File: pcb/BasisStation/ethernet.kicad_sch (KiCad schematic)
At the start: 35 parts, among them T1 7499011121A, U7 W5500, Y1 25 MHz

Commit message: v0.00.001 feat(SHBS-17): Teilenummern fuer 29 Positionen in den Schaltplan uebernommen
Die vom Bediener freigegebenen Teilevorschlaege (Hausstandard Passivteile, LEDs, Q1-Q4, F1, FB1) stehen jetzt als Felder Manufacturer, Manufacturer_Part_Number und Mouser Part Number an 58 Instanzen. F1-Wert von Fuse auf 1.1A gesetzt. Gegenprobe: keine Felder verloren, Netzliste identisch (102 Netze), ERC 0 Fehler.

Stueckliste gruppiert jetzt nach Herstellerteilenummer (Werte sind uneinheitlich geschrieben): 44 Positionen, alle lieferbar, 47,78 EUR. PROPOSED_PARTS geleert, Hausstandard in hardware.md dokumentiert, Bestellteile in power_supply.md aktualisiert.

Co-Authored-By: Claude Opus 5.5 <noreply@anthropic.com>
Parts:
- C16, C17, C18, C19, C20, C21, C22: Manufacturer (none) -> YAGEO; Manufacturer_Part_Number (none) -> CC0805KRX7R9BB104; Mouser Part Number (none) -> 603-CC805KRX7R9BB104
- C23: Manufacturer (none) -> Samsung; Manufacturer_Part_Number (none) -> CL21A475KAQNNNE; Mouser Part Number (none) -> 187-CL21A475KAQNNNE
- C24, C31: Manufacturer (none) -> YAGEO; Manufacturer_Part_Number (none) -> CC0805KRX7R9BB103; Mouser Part Number (none) -> 603-CC805KRX7R9BB103
- C25, C26: Manufacturer (none) -> YAGEO; Manufacturer_Part_Number (none) -> CC0805JRNPO9BN270; Mouser Part Number (none) -> 603-CC805JRNPO9BN270
- C27: Manufacturer (none) -> Samsung; Manufacturer_Part_Number (none) -> CL21B106KOQNNNE; Mouser Part Number (none) -> 187-CL21B106KOQNNNE
- C28: Manufacturer (none) -> KEMET; Manufacturer_Part_Number (none) -> C1206C102KGRACTU; Mouser Part Number (none) -> 80-C1206C102KGR
- C29, C30: Manufacturer (none) -> YAGEO; Manufacturer_Part_Number (none) -> CC0805KRX7R9BB682; Mouser Part Number (none) -> 603-CC805KRX7R9BB682
- C32: Manufacturer (none) -> Samsung; Manufacturer_Part_Number (none) -> CL21B223KBANNNC; Mouser Part Number (none) -> 187-CL21B223KBANNNC
- FB1: Manufacturer (none) -> Murata; Manufacturer_Part_Number (none) -> BLM21PG601SN1D; Mouser Part Number (none) -> 81-BLM21PG601SN1D
- R27: Manufacturer (none) -> YAGEO; Manufacturer_Part_Number (none) -> RC0805FR-0712K4L; Mouser Part Number (none) -> 603-RC0805FR-0712K4L
- R28, R29, R30, R31, R32: Manufacturer (none) -> YAGEO; Manufacturer_Part_Number (none) -> RC0805FR-0710KL; Mouser Part Number (none) -> 603-RC0805FR-0710KL
- R33, R34: Manufacturer (none) -> YAGEO; Manufacturer_Part_Number (none) -> RC0805FR-07220RL; Mouser Part Number (none) -> 603-RC0805FR-07220RL
- R35: Manufacturer (none) -> YAGEO; Manufacturer_Part_Number (none) -> RC0805JR-070RL; Mouser Part Number (none) -> 603-RC0805JR-070RL
- R36, R37, R39, R40: Manufacturer (none) -> YAGEO; Manufacturer_Part_Number (none) -> RC0805FR-0749R9L; Mouser Part Number (none) -> 603-RC0805FR-0749R9L
- R38: Manufacturer (none) -> YAGEO; Manufacturer_Part_Number (none) -> RC0805FR-0710RL; Mouser Part Number (none) -> 603-RC0805FR-0710RL

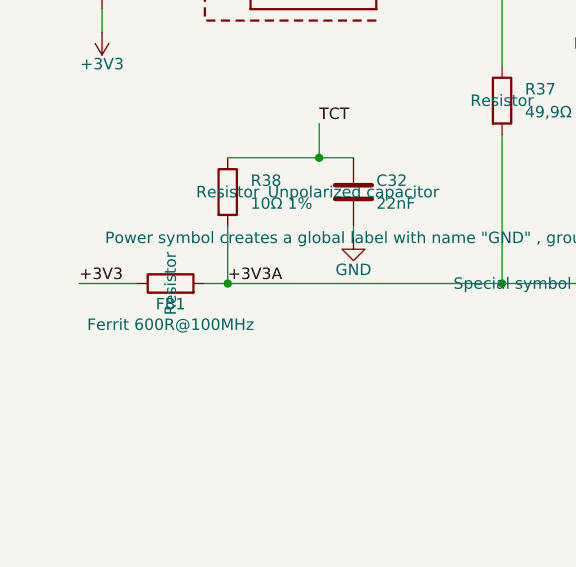
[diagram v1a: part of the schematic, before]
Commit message: v0.00.001 fix(SHBS-16): D10-Verpolung behoben, LED-Symbole vereinheitlicht, FB1 und J6 bereinigt
Footprint WL-TMRC_3MM hatte Pad 1 = Anode, Device:LED hat Pin 1 = Kathode: D10 lag mit der Kathode an +3V3 und haette nie geleuchtet. Footprint auf Pad 1 = K / Pad 2 = A umnummeriert (wie WL-TMRW_3MM), Wuerth-Symbol mitgezogen. D7 von WL-TMRC_3MM auf Device:LED, so platziert, dass K/A auf den bisherigen Drahtenden liegen. FB1 auf Device:FerriteBead, J6-Wert auf 61200621621.

Gegenprobe: ERC 0 Fehler; Netzliste mit gleichen Bauteilen je Netz, nur D7-Pinnummern getauscht; Polaritaet aller vier LEDs auf Pad-Ebene geprueft. Beim naechsten PCB-Abgleich Footprint von D7/D10 aus der Bibliothek aktualisieren. Task 0042 abgeschlossen.

Co-Authored-By: Claude Opus 5.5 <noreply@anthropic.com>
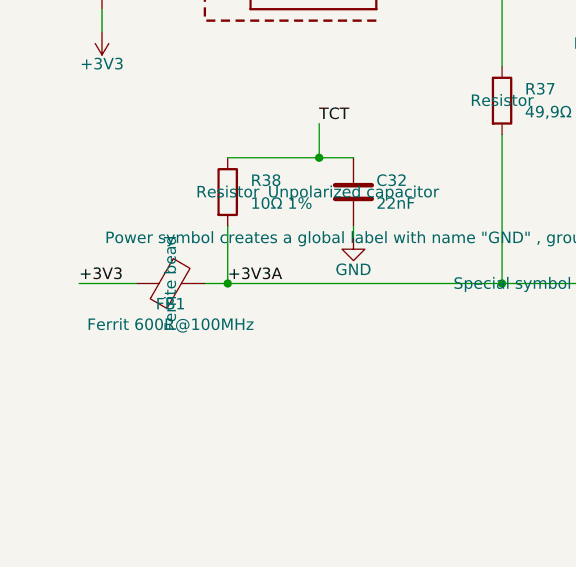
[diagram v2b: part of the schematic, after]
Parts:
- FB1: symbol Device:R -> Device:FerriteBead
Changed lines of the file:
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@@
 	)
 	(symbol
-		(lib_id "Device:R")
+		(lib_id "Device:FerriteBead")
 		(at 41.91 116.84 90)
 		(unit 1)
@@
 			)
 		)
-		(property "Description" "Resistor"
+		(property "Description" "Ferrite bead"
 			(at 41.91 116.84 0)
 			(effects
